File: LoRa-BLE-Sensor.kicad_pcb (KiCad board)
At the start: 4 copper layers, 96 x 85 mm, 108 parts, among them J1 SHF-105-01-X-D-SM, J2 Battery_Cell, J3 Conn_01x06_Socket, J5 Screw_Terminal_01x06, J6 Screw_Terminal_01x06, J7 Conn_01x10_Pin, Q1 DMN67D7L, Q10 SQ2389ES, Q11 DMN62D0UDW-7, Q12 DMN62D0UDW-7, Q2 DMN67D7L, Q5 DMN67D7L, Q6 DMN67D7L, Q9 SQ2389ES, SW1 SW_Push, SW2 SW_Push, SW3 SW_Push, U1 RAK4630, U2 NPM1300-QEAA-R, U3 TLV61046ADBVR, U4 TLV61046ADBVR

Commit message: update
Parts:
- added C26: 300p, Capacitor_SMD:C_0402_1005Metric, F.Cu at (46.5, 92.2)
- added C27: 300p, Capacitor_SMD:C_0402_1005Metric, F.Cu at (46.5, 94.2)
- added Q3: DMN67D7L, Package_TO_SOT_SMD:SOT-23, F.Cu at (42.6, 89.6)
- added Q4: DMN67D7L, Package_TO_SOT_SMD:SOT-23, F.Cu at (42.6, 94.2)
- added Q7: DMN67D7L, Package_TO_SOT_SMD:SOT-23, F.Cu at (42.6, 98.9)
- added Q8: DMN67D7L, Package_TO_SOT_SMD:SOT-23, F.Cu at (42.6, 103.5)
- added R3: 0R, Inductor_SMD:L_0402_1005Metric, F.Cu at (46.5, 88.2)
- added R4: 0R, Inductor_SMD:L_0402_1005Metric, F.Cu at (46.5, 90.2)
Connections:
- net D0_NRF renamed SENSOR1_D1_NRF
- net D1_NRF renamed SENSOR1_D2_NRF
- net D2_NRF renamed SENSOR2_D1_NRF
- net D3_NRF renamed SENSOR2_D2_NRF
- net V_RELAY renamed V_BUCK1
- Q1 pad 3: SENSOR1_D1 -> Net-(Q1-D)
- Q2 pad 3: SENSOR1_D2 -> Net-(Q2-D)
- Q5 pad 3: SENSOR2_D1 -> Net-(Q5-D)
- Q6 pad 3: SENSOR2_D2 -> Net-(Q6-D)
- R13 pad 1: VOUT_SENSOR2 -> V_SENSOR2
- R14 pad 1: VOUT_SENSOR2 -> V_SENSOR2
- R5 pad 1: VOUT_SENSOR1 -> V_SENSOR1
- R6 pad 1: VOUT_SENSOR1 -> V_SENSOR1
- U1 pad 11: NPM_IO2 -> unconnected-(U1-P0.21-Pad11)
- U1 pad 12: NPM_IO1 -> NFC2
- U1 pad 13: BUT1 -> NFC1

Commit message: renaming pin labels
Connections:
- net I0_NRF renamed SENSOR1_IIN_NRF
- net I1_NRF renamed SENSOR2_IIN_NRF
- net V0_NRF renamed SENSOR1_VIN_NRF
- net V1_NRF renamed SENSOR2_VIN_NRF
- Q3 pad 1: V_SENSOR1 -> VOUT_SENSOR1
- Q4 pad 1: V_SENSOR1 -> VOUT_SENSOR1
- Q7 pad 1: V_SENSOR2 -> VOUT_SENSOR2
- Q8 pad 1: V_SENSOR2 -> VOUT_SENSOR2
- R13 pad 1: V_SENSOR2 -> VOUT_SENSOR2
- R14 pad 1: V_SENSOR2 -> VOUT_SENSOR2
- R5 pad 1: V_SENSOR1 -> VOUT_SENSOR1
- R6 pad 1: V_SENSOR1 -> VOUT_SENSOR1

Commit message: added sensor 3
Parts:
- removed R31, R32, R33, R34: 300K, Resistor_SMD:R_0402_1005Metric
- removed REF** (x4): MountingHole_3.2mm_M3_ISO7380, MountingHole:MountingHole_3.2mm_M3_ISO7380
- added C28: 10u, Capacitor_SMD:C_0603_1608Metric, F.Cu at (193.4, 52.6)
- added C29: 10u, Capacitor_SMD:C_0805_2012Metric, F.Cu at (191.6, 60.0)
- added D3: BAT54W-HG3-08, User_Actives:SOD3716X135N, F.Cu at (178.2, 53.6)
- added D7: PRTR5V0U2X,215, User_Actives:PRTR5V0U2X, F.Cu at (183.8, 58.2)
- added J4: Screw_Terminal_01x04, Connector_Phoenix_MC:PhoenixContact_MCV_1,5_4-G-3.81_1x04_P3.81mm_Vertical, F.Cu at (178.8, 47.4)
- added L5: 10U, Inductor_SMD:L_1008_2520Metric, F.Cu at (188.9, 53.3)
- added Q13: SQ2389ES, Package_TO_SOT_SMD:SOT-23-3, F.Cu at (183.8, 53.8)
- added R11: 71K5, Resistor_SMD:R_0402_1005Metric, F.Cu at (187.9, 60.1)
- added R7: 10K, Resistor_SMD:R_0402_1005Metric, F.Cu at (187.9, 56.1)
- added R8: 383K, Resistor_SMD:R_0402_1005Metric, F.Cu at (187.9, 58.1)
- added U5: TLV61046ADBVR, User_Power:SOT95P280X145-6N, F.Cu at (178.4, 58.0)
- moved C26 14.7 mm to (46.0, 77.5)
- moved C27 14.7 mm to (46.0, 79.5)
- moved R3 14.7 mm to (46.0, 73.6)
- moved R4 14.7 mm to (46.0, 75.5)
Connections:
- Q10 pad 1: Net-(Q10-G) -> VBOOST2
- Q9 pad 1: Net-(Q9-G) -> VBOOST1
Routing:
- net VBOOST2: track 26.0 -> 28.7 mm
- net Net-(Q10-G): track 2.79 -> 0.00 mm
- net Net-(Q9-G): track 2.78 -> 0.00 mm
- net VBOOST1: track 35.5 -> 38.3 mm

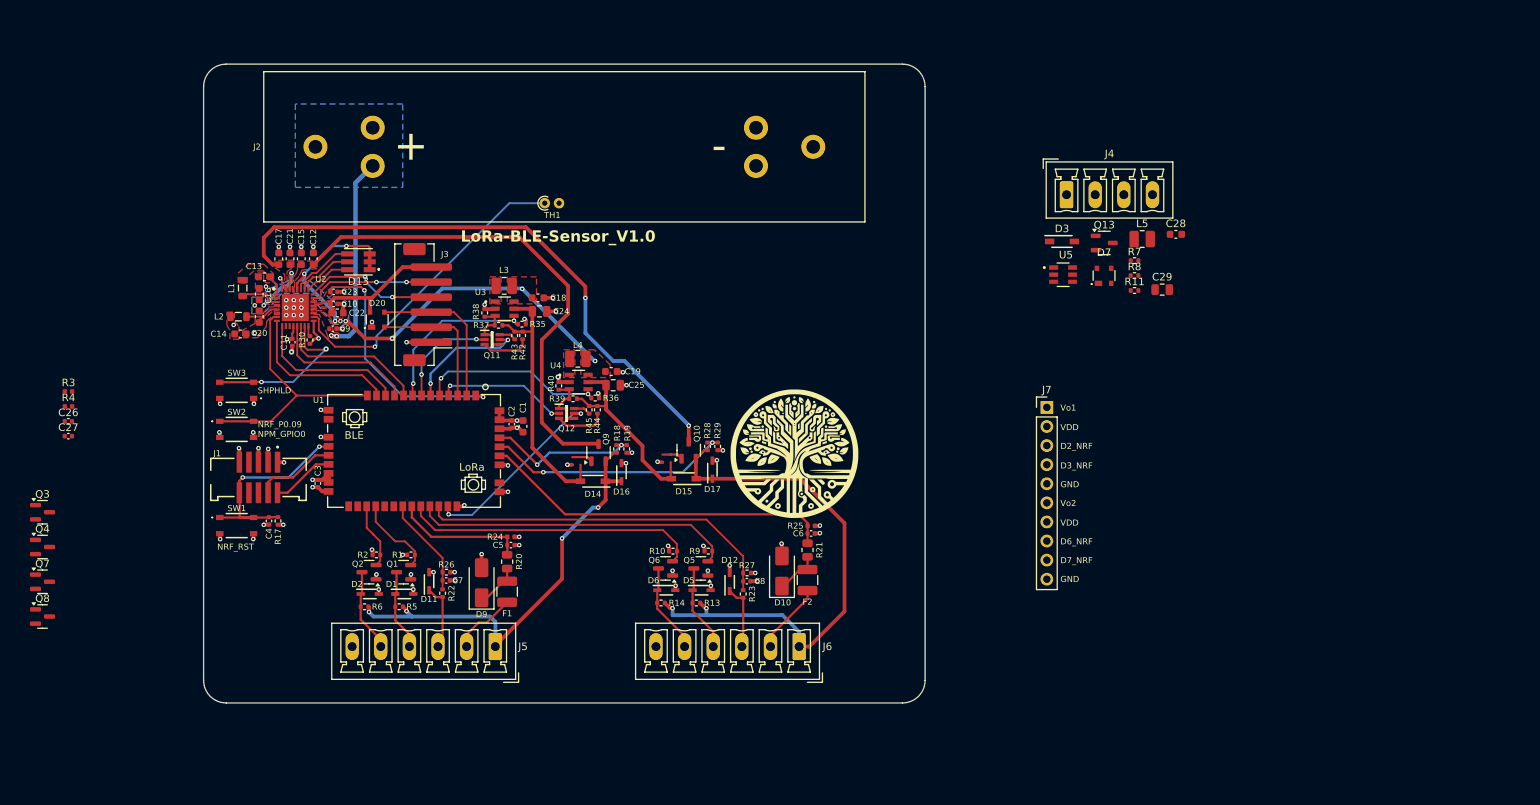
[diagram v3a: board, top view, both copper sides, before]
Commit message: sensor3 schematic almost done
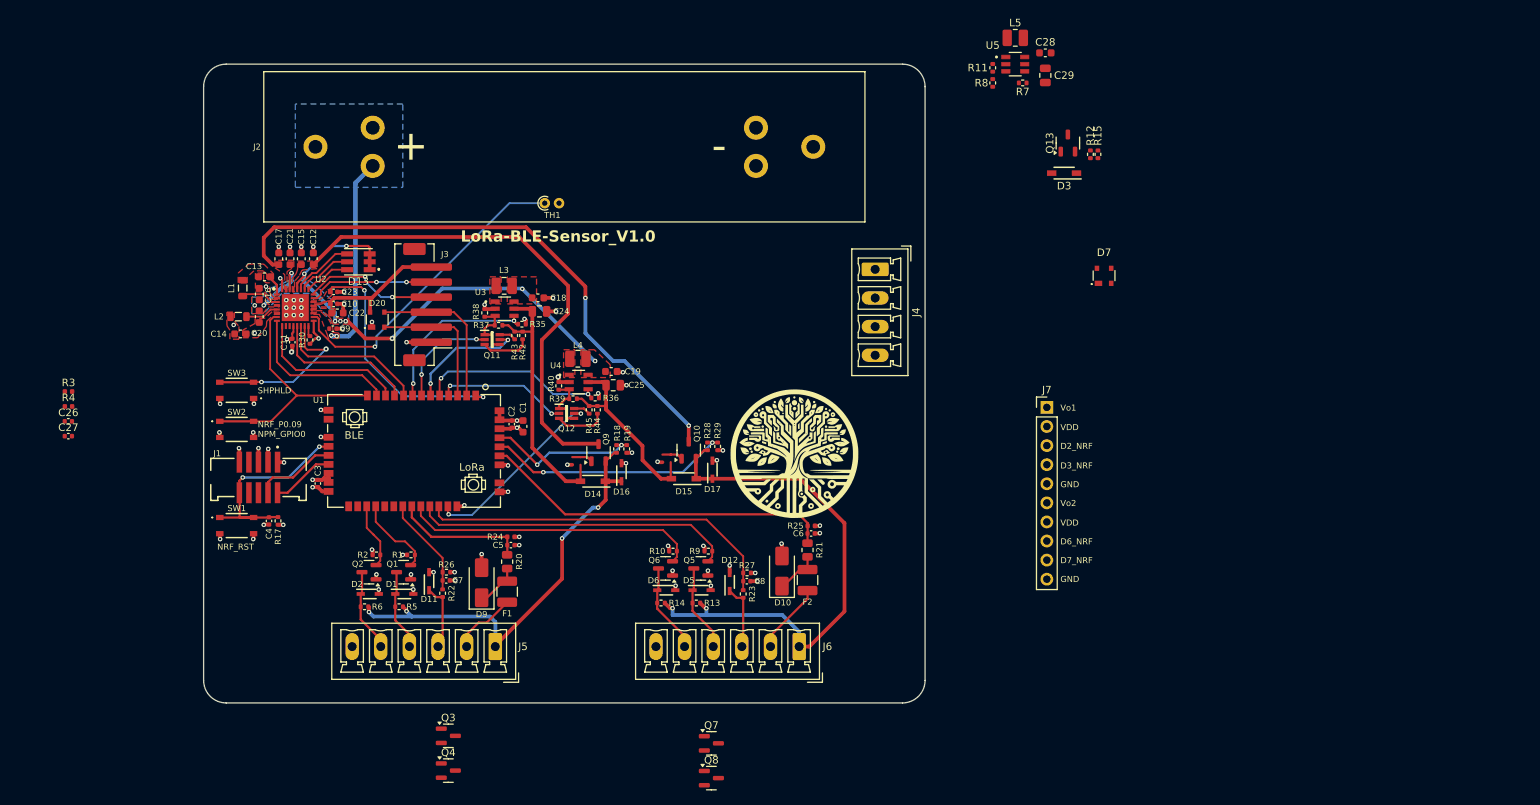
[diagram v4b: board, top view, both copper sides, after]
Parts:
- added R12: 1M, Resistor_SMD:R_0402_1005Metric, F.Cu at (182.0, 42.0)
- added R15: 130K, Resistor_SMD:R_0402_1005Metric, F.Cu at (183.0, 42.0)
- R18, R28: value 100K -> 1M
- R19, R29: value 13K -> 130K
- moved Q7 91.6 mm to (131.6, 120.4)
- moved Q8 91.6 mm to (131.6, 125.0)
- moved Q3 61.7 mm to (96.6, 119.4)
- moved Q4 61.7 mm to (96.6, 124.0)
- moved R11 35.1 mm to (169.0, 30.5), turned to 90 degrees
- moved C29 32.5 mm to (176.0, 31.5), turned to -90 degrees
- moved R8 31.8 mm to (169.0, 32.5), turned to -90 degrees
- moved L5 31.7 mm to (172.0, 26.5), turned to 180 degrees
- moved C28 29.7 mm to (176.0, 28.5)
- moved U5 28.7 mm to (172.0, 30.0)
- moved R7 27.9 mm to (173.0, 32.5), turned to 180 degrees
- moved J4 27.3 mm to (153.4, 57.3), turned to -90 degrees
- moved Q13 14.1 mm to (179.0, 40.5), turned to 90 degrees
- moved D3 9.10 mm to (178.5, 44.5), turned to 180 degrees
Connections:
- D14 pad 1: VOUT_SENSOR1 -> SENSOR1_PWR
- D15 pad 1: VOUT_SENSOR2 -> SENSOR2_PWR
- D16 pad 1: VOUT_SENSOR1 -> SENSOR1_PWR
- D17 pad 1: VOUT_SENSOR2 -> SENSOR2_PWR
- D3 pad 1: VOUT_SENSOR3 -> SENSOR3_PWR
- J4 pad 1: VOUT_SENSOR3 -> SENSOR3_PWR
- J5 pad 1: VOUT_SENSOR1 -> SENSOR1_PWR
- J6 pad 1: VOUT_SENSOR2 -> SENSOR2_PWR
- Q10 pad 2: VOUT_SENSOR2 -> SENSOR2_PWR
- Q13 pad 2: VOUT_SENSOR3 -> SENSOR3_PWR
- Q9 pad 2: VOUT_SENSOR1 -> SENSOR1_PWR
- R18 pad 1: VOUT_SENSOR1 -> SENSOR1_PWR
- R28 pad 1: VOUT_SENSOR2 -> SENSOR2_PWR

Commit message: Beginning routing V1.1
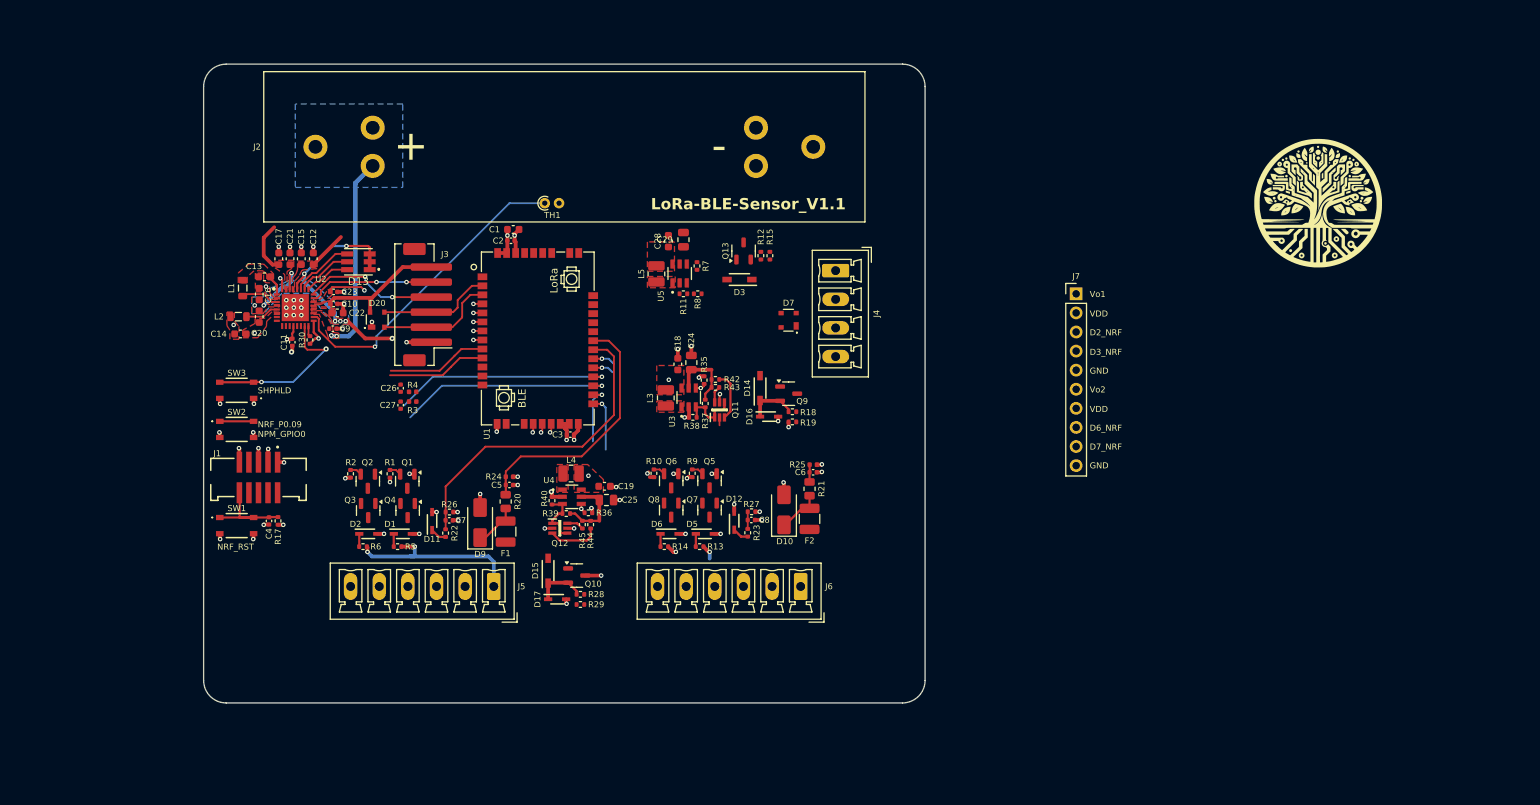
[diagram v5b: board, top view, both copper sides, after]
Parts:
- moved G*** 77.2 mm to (212.4, 48.4)
- moved L5 57.2 mm to (124.2, 57.9), turned to -90 degrees
- moved C28 56.1 mm to (125.8, 53.6), turned to 90 degrees
- moved C29 52.9 mm to (127.8, 53.4), turned to 90 degrees
- moved U5 52.6 mm to (127.3, 57.9), turned to 90 degrees
- moved R11 51.0 mm to (127.8, 60.6), turned to 180 degrees
- moved R7 49.7 mm to (129.7, 56.9), turned to -90 degrees
- moved R8 48.2 mm to (129.8, 60.6), turned to 180 degrees
- moved R12 45.9 mm to (138.2, 55.5)
- moved R4 45.8 mm to (91.8, 73.6), turned to 180 degrees
- moved R3 45.8 mm to (91.8, 74.9), turned to 180 degrees
- moved R15 45.7 mm to (139.3, 55.5)
- moved Q13 45.5 mm to (135.8, 54.9)
- moved D3 45.5 mm to (135.3, 58.7)
- moved C26 44.4 mm to (90.2, 73.1), turned to 90 degrees
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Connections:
- U1 pad 11: unconnected-(U1-P0.21-Pad11) -> BUT1
- U1 pad 23: unconnected-(U1-P0.24-Pad23) -> BOOST2_FB_CTRL1
- U1 pad 24: unconnected-(U1-P0.25-Pad24) -> BOOST2_FB_CTRL2
- U1 pad 25: SENSOR1_D2_NRF -> SENSOR1_D1_NRF
- U1 pad 26: SENSOR1_D1_NRF -> SENSOR1_D2_NRF
- U1 pad 27: unconnected-(U1-P1.03-Pad27) -> SENSOR2_D2_NRF
- U1 pad 28: unconnected-(U1-P1.04-Pad28) -> SENSOR2_D1_NRF
- U1 pad 31: SENSOR2_D2_NRF -> SENSOR2_VIN_NRF
- U1 pad 32: SENSOR2_D1_NRF -> SENSOR2_IIN_NRF
- U1 pad 33: SENSOR2_VIN_NRF -> SENSOR3_D2_NRF
- U1 pad 34: BOOST2_FB_CTRL1 -> SENSOR3_D1_NRF
- U1 pad 39: SENSOR2_IIN_NRF -> V_SENSOR3_READ
- U1 pad 4: BOOST2_FB_CTRL2 -> BOOST3_EN
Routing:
- net LDO2_OUT: track 78.7 -> 8.99 mm, vias 2 -> 1
- net VOUT_SENSOR2: track 70.6 -> 3.37 mm
- net LDO1_OUT: track 66.5 -> 5.20 mm
- net SENSOR2_VIN_NRF: track 48.5 -> 2.29 mm
- net SENSOR2_IIN_NRF: track 47.4 -> 2.31 mm
- net SENSOR2_D1_NRF: track 42.8 -> 4.64 mm, vias 0 -> 1
- net SENSOR2_D2_NRF: track 39.4 -> 4.40 mm, vias 0 -> 1
- net VSYS: track 73.1 -> 39.2 mm
- net VOUT_SENSOR1: track 58.1 -> 24.9 mm, vias 4 -> 2
- net V_SENSOR2_READ: track 32.7 -> 0.00 mm, vias 2 -> 0
- net SENSOR1_VIN_NRF: track 13.3 -> 43.0 mm
- net BUT1: track 33.6 -> 4.50 mm
- net VBOOST1: track 38.3 -> 9.62 mm
- net VBUS_NRF: track 33.2 -> 5.21 mm, vias 2 -> 1
- net BOOST2_EN: track 24.9 -> 2.50 mm
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- added copper zone on F.Cu, net Net-(U5-SW)
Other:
- board text added: "LoRa-BLE-Sensor_V1.1"
- board text removed: "LoRa-BLE-Sensor_V1.0"

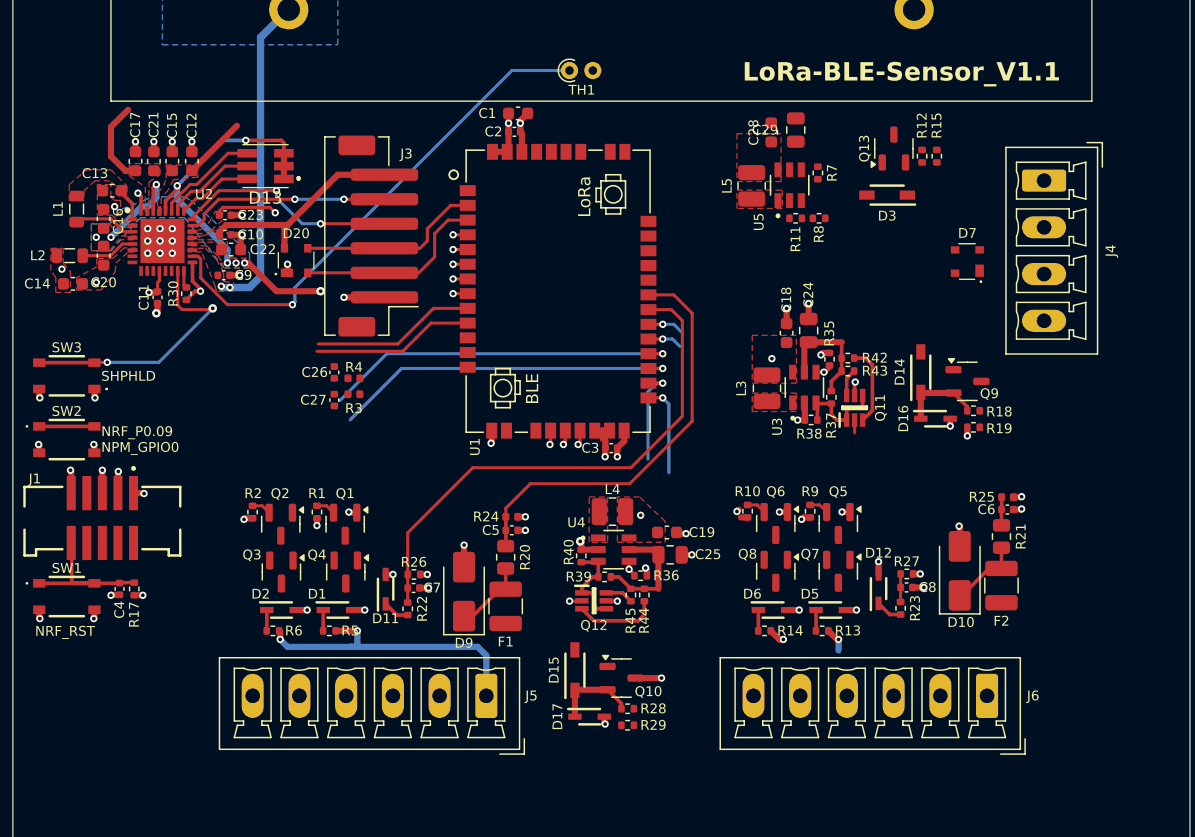
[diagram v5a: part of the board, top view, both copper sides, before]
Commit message: labels fixed
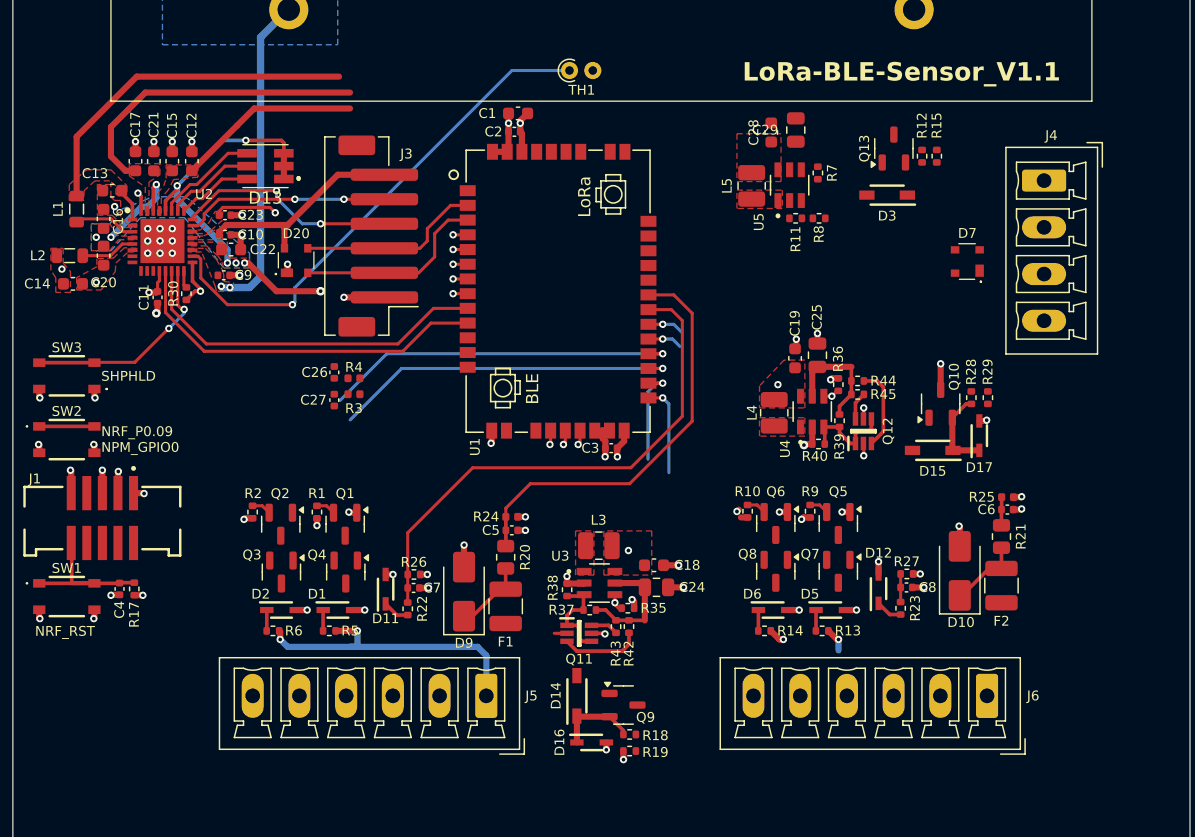
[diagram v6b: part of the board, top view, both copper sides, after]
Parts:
- moved R29 39.7 mm to (143.5, 75.2), turned to -90 degrees
- moved D17 39.2 mm to (142.8, 78.3), turned to 90 degrees
- moved D14 38.5 mm to (110.0, 99.5)
- moved D16 38.5 mm to (111.2, 103.3)
- moved Q9 38.5 mm to (113.8, 100.2)
- moved R18 38.5 mm to (114.3, 102.7)
- moved R19 38.5 mm to (114.3, 104.0)
- moved R28 37.8 mm to (142.2, 75.2), turned to 90 degrees
- moved Q10 34.3 mm to (139.7, 75.7), turned to 90 degrees
- moved D15 34.2 mm to (139.0, 79.5), turned to 180 degrees
- moved Q11 29.0 mm to (110.2, 94.4), turned to 0 degrees
- moved R42 28.3 mm to (114.2, 93.8), turned to -90 degrees
- moved R43 28.1 mm to (113.2, 93.8), turned to -90 degrees
- moved R37 26.3 mm to (111.0, 92.5), turned to 180 degrees
- moved R35 26.1 mm to (114.2, 92.3), turned to 0 degrees
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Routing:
- net V_BUCK1: track 2.51 -> 30.8 mm
- net LDO2_OUT: track 8.99 -> 27.7 mm
- net NPM_SDA: track 13.2 -> 30.3 mm
- net NPM_SCL: track 13.4 -> 29.6 mm
- net LDO1_OUT: track 5.20 -> 15.0 mm
- net Net-(U2-SHPHLD): track 21.9 -> 17.3 mm

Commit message: signal routing
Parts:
- added G***: LOGO, User_Images:DOE_LOGO_10mm, F.Cu at (43.2, 49.6)
- moved G*** 100.6 mm to (112.1, 40.9)
- moved J7 16.7 mm to (172.5, 75.5)
- moved TH1 11.8 mm to (97.6, 48.5)
- moved C27 1.15 mm to (89.1, 75.7)
- moved C26 1.15 mm to (89.1, 73.4)
- moved R4 1.15 mm to (90.7, 73.9)
- moved R3 1.15 mm to (90.7, 75.2)
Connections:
- U1 pad 23: BOOST2_FB_CTRL1 -> BOOST1_FB_CTRL1
- U1 pad 24: BOOST2_FB_CTRL2 -> BOOST1_FB_CTRL2
- U1 pad 6: BOOST1_FB_CTRL1 -> BOOST2_FB_CTRL1
- U1 pad 7: BOOST1_FB_CTRL2 -> BOOST2_FB_CTRL2
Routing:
- net LDO1_OUT: track 15.0 -> 76.0 mm, vias 0 -> 4
- net V_BUCK1: track 30.8 -> 78.7 mm
- net RESET: track 14.1 -> 57.6 mm, vias 1 -> 2
- net SWCLK: track 1.19 -> 41.7 mm, vias 1 -> 0
- net SWDIO: track 1.19 -> 40.8 mm, vias 1 -> 0
- net SENSOR2_PWR: track 6.85 -> 33.7 mm
- net LDO2_OUT: track 27.7 -> 45.2 mm
- net VBUS_NRF: track 5.21 -> 21.6 mm, vias 1 -> 2
- net VBOOST2: track 9.63 -> 21.4 mm
- net BOOST1_EN: track 2.67 -> 14.2 mm, vias 2 -> 4
- net VBOOST1: track 9.62 -> 21.0 mm
- net SENSOR1_PWR: track 6.75 -> 14.8 mm
- net Net-(U2-NTC): track 41.9 -> 34.3 mm
- net SENSOR1_D1_NRF: track 30.0 -> 37.2 mm
- net BOOST2_FB_CTRL2: track 9.17 -> 2.21 mm
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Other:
- board size 96 x 85 mm -> 96 x 80 mm
- board text added: "SENSOR 1 POWER OUTPUTS: 0V, 3.3V, 5V, 6V, 12V, 24V SENSOR INPUTS: Voltage(0-28V), Current(4-20mA), Digital Input"
- board text added: "SENSOR 2 POWER OUTPUTS: 0V, 3.3V, 5V, 6V, 12V, 24V SENSOR INPUTS: Voltage(0-28V), Current(4-20mA), Digital Input"
- board text added: "SENSOR 3 POWER OUTPUTS: 0V, 3.3V, 5V SENSOR INPUTS: Digital Input"
